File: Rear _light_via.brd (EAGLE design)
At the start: 59.8 x 72.7 mm, 9 parts

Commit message: via gerbers generated
via boards completed and gerbers generated
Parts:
- moved L_SIG 57.5 mm to (59.7, 13.4)
- moved REAR 53.5 mm to (5.21, 38.9), turned to 270 degrees
- moved H1 40.3 mm to (3.85, 3.85)
- moved H2 40.3 mm to (56.0, 3.85)
- moved H3 40.3 mm to (3.85, 68.8)
- moved H4 40.3 mm to (56.2, 68.8)
- moved L_DRIVE 34.0 mm to (59.7, 43.2)
- moved T_DRIVE 33.7 mm to (59.7, 28.3)
- moved R_SIG 32.2 mm to (59.7, 58.6)
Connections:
- net N$4 renamed BRAKE_L
- net N$5 renamed DRIVE_R
- net N$6 renamed BRAKE_R
- net N$8 renamed DRIVE_L
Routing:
- net N$3: track 23.1 -> 49.0 mm
- net DRIVE_R: track 25.6 -> 42.3 mm
- net N$2: track 35.7 -> 49.1 mm
- net N$7: track 43.5 -> 56.7 mm
- net N$1: track 32.3 -> 41.3 mm
- net DRIVE_L: track 37.6 -> 42.0 mm
- net BRAKE_R: track 44.8 -> 47.7 mm, vias 0 -> 1
- net BRAKE_L: track 45.5 -> 46.5 mm
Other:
- board text added: "BRAKE_L"
- board text added: "BRAKE_R"
- board text added: "DRIVE_L"
- board text added: "DRIVE_R"

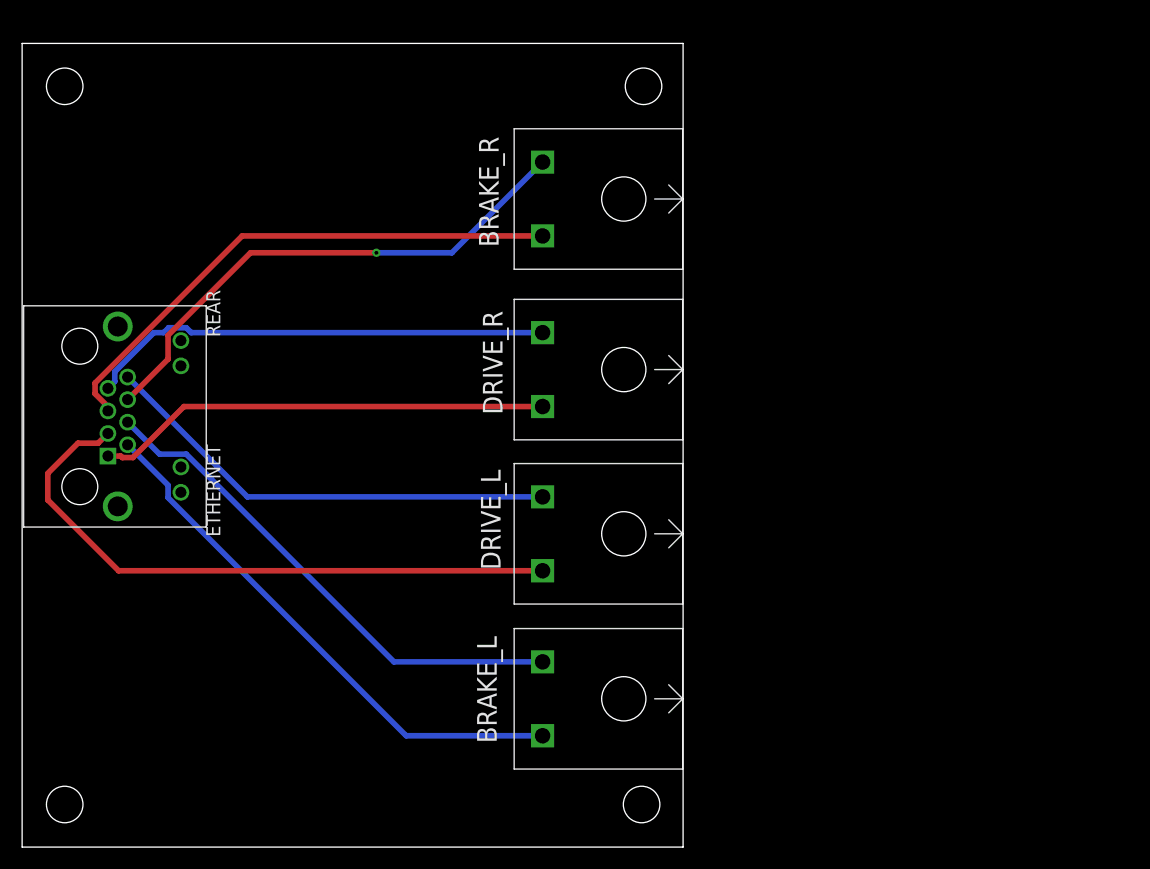
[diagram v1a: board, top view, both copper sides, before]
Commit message: added reverse polairity protection
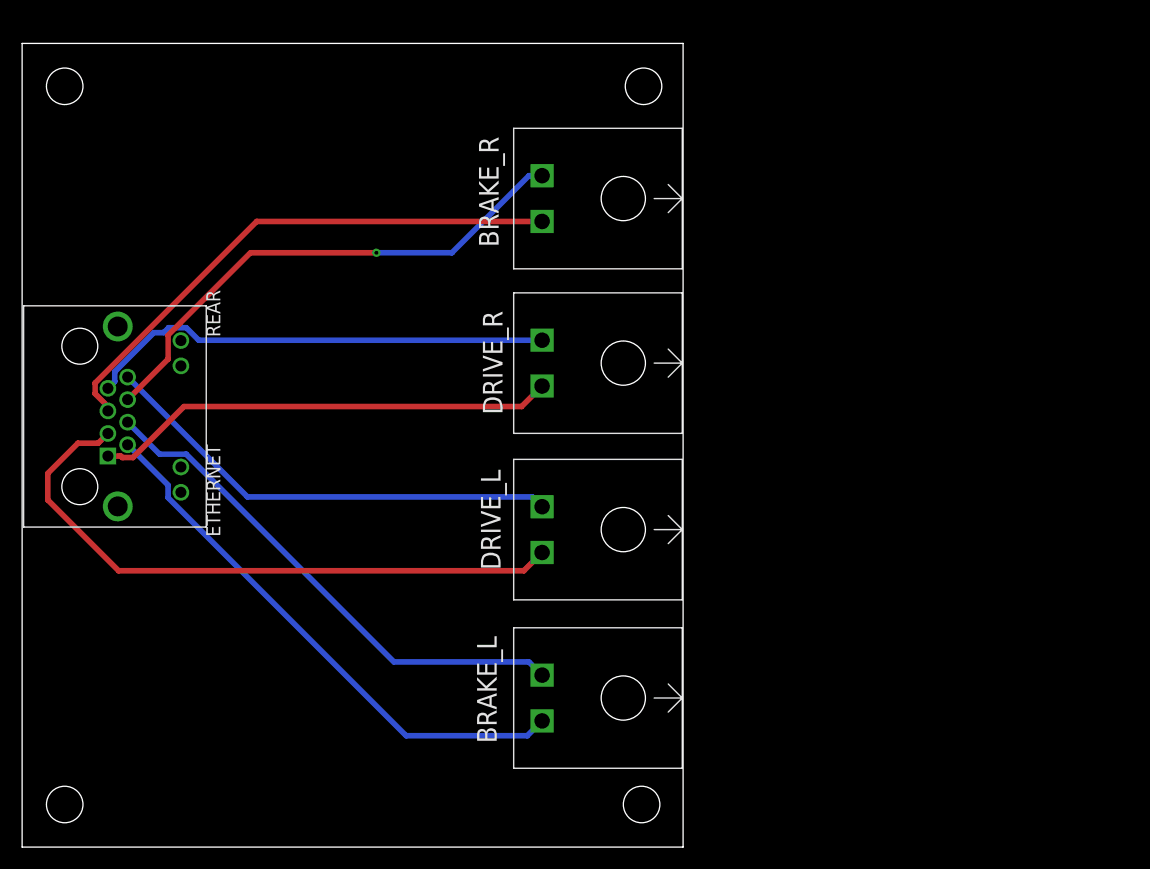
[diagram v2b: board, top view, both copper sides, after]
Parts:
- removed L_DRIVE, L_SIG, R_SIG, T_DRIVE: 2_PIN_TECONNECTOR, TE 2-pin connector:2_PIN_CONNECT
- added U$1, U$2, U$3, U$4: 2_PIN_TECONNECTOR, TE 2-pin connector:2_PIN_CONNECT
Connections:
- net BRAKE_L: now also U$3.G/LOW; no longer L_SIG.G/LOW
- net BRAKE_R: now also U$2.G/LOW; no longer R_SIG.G/LOW
- net DRIVE_L: now also U$1.G/LOW; no longer T_DRIVE.G/LOW
- net DRIVE_R: now also U$4.G/LOW; no longer L_DRIVE.G/LOW
- net N$1: now also U$4.V/SIG; no longer L_DRIVE.V/SIG
- net N$2: now also U$3.V/SIG; no longer L_SIG.V/SIG
- net N$3: now also U$2.V/SIG; no longer R_SIG.V/SIG
- net N$7: now also U$1.V/SIG; no longer T_DRIVE.V/SIG
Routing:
- net N$1: track 41.3 -> 42.0 mm
- net N$7: track 56.7 -> 57.3 mm
- net BRAKE_R: track 47.7 -> 47.1 mm
- net N$2: track 49.1 -> 49.6 mm
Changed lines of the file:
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@@
 <?xml version="1.0" encoding="utf-8"?>
 <!DOCTYPE eagle SYSTEM "eagle.dtd">
-<eagle version="8.6.0">
+<eagle version="8.6.1">
 <drawing>
 <settings>
@@
 </autorouter>
 <elements>
-<element name="L_DRIVE" library="TE 2-pin connector" package="2_PIN_CONNECT" value="2_PIN_TECONNECTOR" x="59.72" y="43.165" rot="R90"/>
-<element name="L_SIG" library="TE 2-pin connector" package="2_PIN_CONNECT" value="2_PIN_TECONNECTOR" x="59.72" y="13.405" rot="R90"/>
 <element name="REAR" library="ETHERNET" package="A122645-ND" value="ETHERNET" x="5.215" y="38.93" rot="R270"/>
-<element name="R_SIG" library="TE 2-pin connector" package="2_PIN_CONNECT" value="2_PIN_TECONNECTOR" x="59.72" y="58.585" rot="R90"/>
-<element name="T_DRIVE" library="TE 2-pin connector" package="2_PIN_CONNECT" value="2_PIN_TECONNECTOR" x="59.72" y="28.32" rot="R90"/>
 <element name="H1" library="SparkFun-Electromechanical" package="STAND-OFF" value="STAND-OFF" x="3.85" y="3.85"/>
 <element name="H2" library="SparkFun-Electromechanical" package="STAND-OFF" value="STAND-OFF" x="56" y="3.85"/>
 <element name="H3" library="SparkFun-Electromechanical" package="STAND-OFF" value="STAND-OFF" x="3.85" y="68.775"/>
 <element name="H4" library="SparkFun-Electromechanical" package="STAND-OFF" value="STAND-OFF" x="56.175" y="68.775"/>
+<element name="U$1" library="TE 2-pin connector" package="2_PIN_CONNECT" value="2_PIN_TECONNECTOR" x="59.675" y="28.7" rot="R90"/>
+<element name="U$2" library="TE 2-pin connector" package="2_PIN_CONNECT" value="2_PIN_TECONNECTOR" x="59.675" y="58.625" rot="R90"/>
+<element name="U$3" library="TE 2-pin connector" package="2_PIN_CONNECT" value="2_PIN_TECONNECTOR" x="59.675" y="13.475" rot="R90"/>
+<element name="U$4" library="TE 2-pin connector" package="2_PIN_CONNECT" value="2_PIN_TECONNECTOR" x="59.675" y="43.75" rot="R90"/>
 </elements>
 <signals>
 <signal name="N$1">
 <contactref element="REAR" pad="P$1"/>
-<contactref element="L_DRIVE" pad="V/SIG"/>
 <wire x1="9.05434375" y1="35.2096" x2="10.01565625" y2="35.2096" width="0.508" layer="1"/>
 <wire x1="7.755" y1="35.35" x2="8.91394375" y2="35.35" width="0.508" layer="1"/>
 <wire x1="8.91394375" y1="35.35" x2="9.05434375" y2="35.2096" width="0.508" layer="1"/>
-<wire x1="14.63105625" y1="39.825" x2="47.05" y2="39.825" width="0.508" layer="1"/>
 <wire x1="10.01565625" y1="35.2096" x2="14.63105625" y2="39.825" width="0.508" layer="1"/>
+<contactref element="U$4" pad="V/SIG"/>
+<wire x1="14.63105625" y1="39.825" x2="45.15" y2="39.825" width="0.508" layer="1"/>
+<wire x1="45.15" y1="39.825" x2="47.005" y2="41.68" width="0.508" layer="1"/>
 </signal>
 <signal name="BRAKE_L">
 <contactref element="REAR" pad="P$4"/>
-<contactref element="L_SIG" pad="G/LOW"/>
 <wire x1="9.535" y1="38.41" x2="12.4246" y2="35.5204" width="0.508" layer="16"/>
 <wire x1="12.4246" y1="35.5204" x2="14.83565625" y2="35.5204" width="0.508" layer="16"/>
-<wire x1="33.61105625" y1="16.745" x2="47.05" y2="16.745" width="0.508" layer="16"/>
 <wire x1="14.83565625" y1="35.5204" x2="33.61105625" y2="16.745" width="0.508" layer="16"/>
+<contactref element="U$3" pad="G/LOW"/>
+<wire x1="33.61105625" y1="16.745" x2="45.805" y2="16.745" width="0.508" layer="16"/>
+<wire x1="45.805" y1="16.745" x2="47.005" y2="15.545" width="0.508" layer="16"/>
 </signal>
 <signal name="BRAKE_R">
 <contactref element="REAR" pad="P$6"/>
-<contactref element="R_SIG" pad="G/LOW"/>
 <via x="32.025" y="53.725" extent="1-16" drill="0.35"/>
 <wire x1="9.535" y1="40.45" x2="13.1946" y2="44.1096" width="0.508" layer="1"/>
@@
 <wire x1="20.64894375" y1="53.725" x2="32.025" y2="53.725" width="0.508" layer="1"/>
 <wire x1="32.025" y1="53.725" x2="38.85" y2="53.725" width="0.508" layer="16"/>
-<wire x1="38.85" y1="53.725" x2="47.05" y2="61.925" width="0.508" layer="16"/>
+<contactref element="U$2" pad="G/LOW"/>
+<wire x1="38.85" y1="53.725" x2="45.82" y2="60.695" width="0.508" layer="16"/>
+<wire x1="45.82" y1="60.695" x2="47.005" y2="60.695" width="0.508" layer="16"/>
 </signal>
 <signal name="DRIVE_L">
 <contactref element="REAR" pad="P$8"/>
-<contactref element="T_DRIVE" pad="G/LOW"/>
 <wire x1="9.535" y1="42.49" x2="20.365" y2="31.66" width="0.508" layer="16"/>
-<wire x1="20.365" y1="31.66" x2="47.05" y2="31.66" width="0.508" layer="16"/>
+<contactref element="U$1" pad="G/LOW"/>
+<wire x1="20.365" y1="31.66" x2="46.115" y2="31.66" width="0.508" layer="16"/>
+<wire x1="46.115" y1="31.66" x2="47.005" y2="30.77" width="0.508" layer="16"/>
 </signal>
 <signal name="N$2">
 <contactref element="REAR" pad="P$2"/>
-<contactref element="L_SIG" pad="V/SIG"/>
 <wire x1="9.535" y1="36.37" x2="13.1946" y2="32.7104" width="0.508" layer="16"/>
 <wire x1="13.1946" y1="32.7104" x2="13.1946" y2="31.58934375" width="0.508" layer="16"/>
 <wire x1="13.1946" y1="31.58934375" x2="34.71894375" y2="10.065" width="0.508" layer="16"/>
-<wire x1="34.71894375" y1="10.065" x2="47.05" y2="10.065" width="0.508" layer="16"/>
+<contactref element="U$3" pad="V/SIG"/>
+<wire x1="34.71894375" y1="10.065" x2="45.665" y2="10.065" width="0.508" layer="16"/>
+<wire x1="45.665" y1="10.065" x2="47.005" y2="11.405" width="0.508" layer="16"/>
 </signal>
 <signal name="N$3">
 <contactref element="REAR" pad="P$5"/>
-<contactref element="R_SIG" pad="V/SIG"/>
 <wire x1="6.5946" y1="40.98934375" x2="6.5946" y2="41.95065625" width="0.508" layer="1"/>
 <wire x1="7.755" y1="39.43" x2="7.755" y2="39.82894375" width="0.508" layer="1"/>
 <wire x1="7.755" y1="39.82894375" x2="6.5946" y2="40.98934375" width="0.508" layer="1"/>
-<wire x1="6.5946" y1="41.95065625" x2="19.88894375" y2="55.245" width="0.508" layer="1"/>
-<wire x1="19.88894375" y1="55.245" x2="47.05" y2="55.245" width="0.508" layer="1"/>
+<contactref element="U$2" pad="V/SIG"/>
+<wire x1="21.19894375" y1="56.555" x2="47.005" y2="56.555" width="0.508" layer="1"/>
+<wire x1="6.5946" y1="41.95065625" x2="21.19894375" y2="56.555" width="0.508" layer="1"/>
 </signal>
 <signal name="DRIVE_R">
 <contactref element="REAR" pad="P$7"/>
-<contactref element="L_DRIVE" pad="G/LOW"/>
 <wire x1="7.755" y1="41.47" x2="8.3746" y2="42.0896" width="0.508" layer="16"/>
 <wire x1="8.3746" y1="42.0896" x2="8.3746" y2="42.97065625" width="0.508" layer="16"/>
-<wire x1="14.83565625" y1="46.9504" x2="15.28105625" y2="46.505" width="0.508" layer="16"/>
-<wire x1="15.28105625" y1="46.505" x2="47.05" y2="46.505" width="0.508" layer="16"/>
 <wire x1="11.90894375" y1="46.505" x2="12.79" y2="46.505" width="0.508" layer="16"/>
 <wire x1="12.79" y1="46.505" x2="13.2354" y2="46.9504" width="0.508" layer="16"/>
 <wire x1="8.3746" y1="42.97065625" x2="11.90894375" y2="46.505" width="0.508" layer="16"/>
 <wire x1="13.2354" y1="46.9504" x2="14.83565625" y2="46.9504" width="0.508" layer="16"/>
+<contactref element="U$4" pad="G/LOW"/>
+<wire x1="15.96605625" y1="45.82" x2="47.005" y2="45.82" width="0.508" layer="16"/>
+<wire x1="14.83565625" y1="46.9504" x2="15.96605625" y2="45.82" width="0.508" layer="16"/>
 </signal>
 <signal name="N$7">
 <contactref element="REAR" pad="P$3"/>
-<contactref element="T_DRIVE" pad="V/SIG"/>
 <wire x1="2.32" y1="33.77915" x2="2.32" y2="31.38085" width="0.508" layer="1"/>
 <wire x1="7.755" y1="37.39" x2="6.8754" y2="36.5104" width="0.508" layer="1"/>
@@
 <wire x1="5.05125" y1="36.5104" x2="2.32" y2="33.77915" width="0.508" layer="1"/>
 <wire x1="2.32" y1="31.38085" x2="8.72085" y2="24.98" width="0.508" layer="1"/>
-<wire x1="8.72085" y1="24.98" x2="47.05" y2="24.98" width="0.508" layer="1"/>
+<contactref element="U$1" pad="V/SIG"/>
+<wire x1="8.72085" y1="24.98" x2="45.355" y2="24.98" width="0.508" layer="1"/>
+<wire x1="45.355" y1="24.98" x2="47.005" y2="26.63" width="0.508" layer="1"/>
 </signal>
 </signals>
